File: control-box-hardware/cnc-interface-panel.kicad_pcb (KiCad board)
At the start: 4 copper layers, 94.6 x 73.7 mm, 52 parts, among them J1 USB_B_Mini, J2 SWD_DAPLINK, J3 3V3-OUT, J4 5V-OUT, J5 GND-OUT, J6 IO-A, J7 IO-B, J8 I2C, SW1 BOOT0, SW2 RESET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

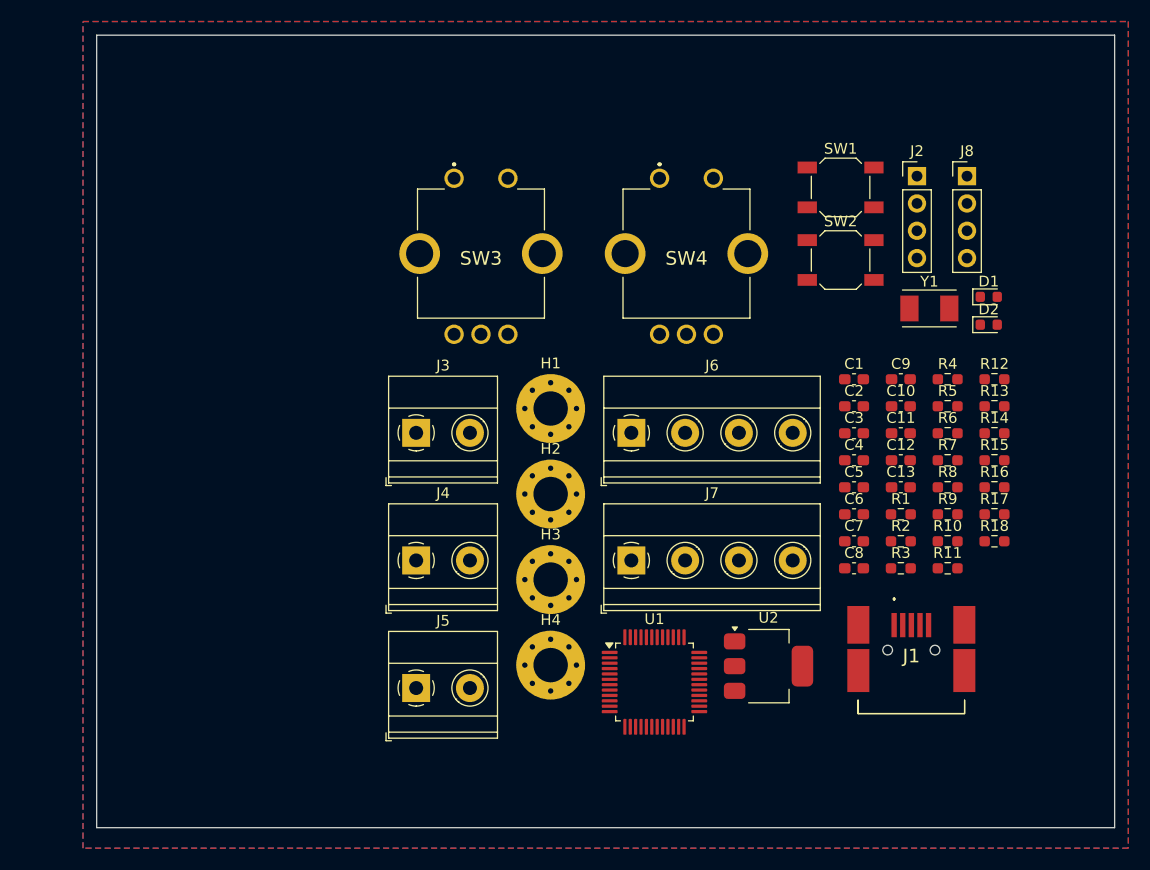
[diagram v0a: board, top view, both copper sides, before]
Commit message: Finish laying out CNC encoders PCB
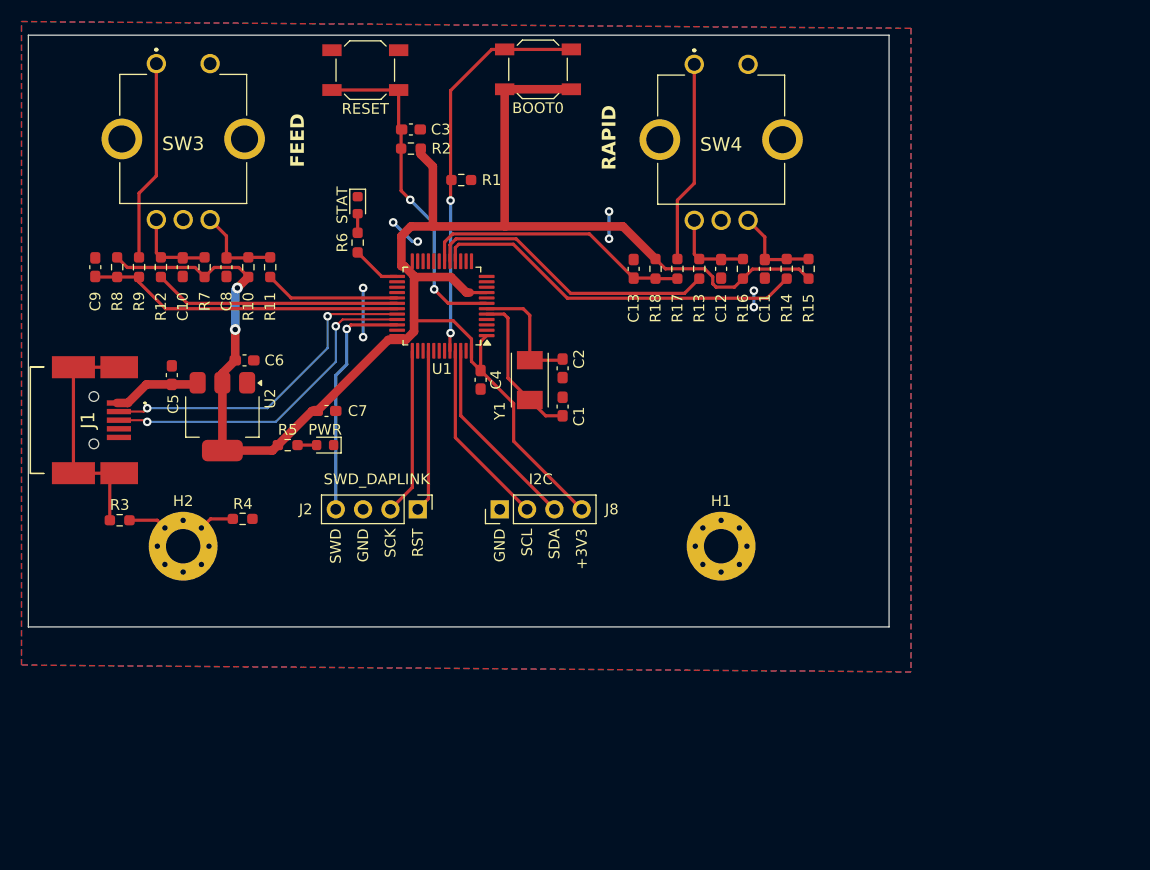
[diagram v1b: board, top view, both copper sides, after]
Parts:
- removed H3, H4: ~, MountingHole:MountingHole_3.2mm_M3_Pad_Via
- removed J3: 3V3-OUT, TerminalBlock_Phoenix:TerminalBlock_Phoenix_MKDS-1,5-2_1x02_P5.00mm_Horizontal
- removed J4: 5V-OUT, TerminalBlock_Phoenix:TerminalBlock_Phoenix_MKDS-1,5-2_1x02_P5.00mm_Horizontal
- removed J5: GND-OUT, TerminalBlock_Phoenix:TerminalBlock_Phoenix_MKDS-1,5-2_1x02_P5.00mm_Horizontal
- removed J6: IO-A, TerminalBlock_Phoenix:TerminalBlock_Phoenix_MKDS-1,5-4_1x04_P5.00mm_Horizontal
- removed J7: IO-B, TerminalBlock_Phoenix:TerminalBlock_Phoenix_MKDS-1,5-4_1x04_P5.00mm_Horizontal
- moved J1 80.7 mm to (82.8, 87.2), turned to -90 degrees
- moved R8 79.9 mm to (86.4, 73.0), turned to -90 degrees
- moved R9 78.6 mm to (88.4, 73.0), turned to 90 degrees
- moved R12 78.2 mm to (90.4, 73.0), turned to 90 degrees
- moved C9 75.6 mm to (84.3, 73.0), turned to 90 degrees
- moved R3 72.7 mm to (86.6, 96.5)
- moved R7 71.4 mm to (94.5, 73.0), turned to 90 degrees
- moved R10 69.8 mm to (98.6, 73.0), turned to 90 degrees
- moved R11 68.9 mm to (100.6, 73.0), turned to 90 degrees
- moved C10 68.0 mm to (92.5, 73.0), turned to -90 degrees
- moved R4 66.8 mm to (98.0, 96.4), turned to 180 degrees
- moved C8 64.7 mm to (96.5, 73.0), turned to -90 degrees
- moved C5 64.3 mm to (91.4, 83.0), turned to 90 degrees
- moved D1 63.2 mm to (105.7, 89.5), turned to 180 degrees
- moved R5 61.4 mm to (102.2, 89.5)
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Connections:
- C3 pad 1: Net-(C3-Pad1) -> Net-(U1-NRST)
- H1 pad 1: CASE -> unconnected-(H1-Pad1)
- J2 pad 1: /SWD -> /RST
- J2 pad 4: /RST -> /SWD
- J8 pad 2: /I2C_SDA -> /I2C_SCL
- J8 pad 3: /I2C_SCL -> /I2C_SDA
- R2 pad 2: Net-(C3-Pad1) -> Net-(U1-NRST)
- SW2 pad 2: Net-(C3-Pad1) -> Net-(U1-NRST)
- U1 pad 10: Net-(J6-Pin_1) -> unconnected-(U1-PA0-Pad10)
- U1 pad 11: Net-(J6-Pin_2) -> unconnected-(U1-PA1-Pad11)
- U1 pad 12: Net-(J6-Pin_3) -> unconnected-(U1-PA2-Pad12)
- U1 pad 13: Net-(J6-Pin_4) -> unconnected-(U1-PA3-Pad13)
- U1 pad 15: /RAPID_RESET -> unconnected-(U1-PA5-Pad15)
- U1 pad 16: /RAPID_A -> /RAPID_B
- U1 pad 17: /RAPID_B -> /RAPID_A
- U1 pad 18: Net-(J7-Pin_1) -> /RAPID_RESET
- U1 pad 19: Net-(J7-Pin_2) -> unconnected-(U1-PB1-Pad19)
- U1 pad 20: Net-(J7-Pin_3) -> unconnected-(U1-PB2-Pad20)
- U1 pad 29: /FEED_A -> /FEED_B
- U1 pad 30: /FEED_B -> /FEED_A
- U1 pad 39: Net-(J7-Pin_4) -> unconnected-(U1-PB3-Pad39)
- U1 pad 7: GND -> Net-(U1-NRST)
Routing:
- net +3V3: track 0.00 -> 168.3 mm, vias 0 -> 2
- net Net-(U1-BOOT0): track 0.00 -> 37.0 mm, vias 0 -> 2
- net /RAPID_B: track 0.00 -> 35.0 mm
- net /D+: track 0.00 -> 32.0 mm, vias 0 -> 2
- net Net-(U1-NRST): track 0.00 -> 31.6 mm, vias 0 -> 2
- net /D-: track 0.00 -> 31.5 mm, vias 0 -> 2
- net /FEED_RESET: track 0.00 -> 29.6 mm
- net /RAPID_A: track 0.00 -> 27.6 mm
- net /RAPID_RESET: track 0.00 -> 25.5 mm
- net Net-(J1-Shield): track 0.00 -> 23.1 mm
- net /FEED_A: track 0.00 -> 23.0 mm
- net /SWD: track 0.00 -> 22.0 mm, vias 0 -> 1
- net Net-(R17-Pad2): track 0.00 -> 18.7 mm
- net Net-(R9-Pad2): track 0.00 -> 18.7 mm
- net /I2C_SDA: track 0.00 -> 18.3 mm
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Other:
- board size 94.6 x 73.7 mm -> 80 x 55 mm
- copper layers 4 -> 2
- board text added: "+3V3"
- board text added: "GND"
- board text added: "RST"
- board text added: "SCK"
- board text added: "SCL"
- board text added: "SDA"
- board text added: "SWD"

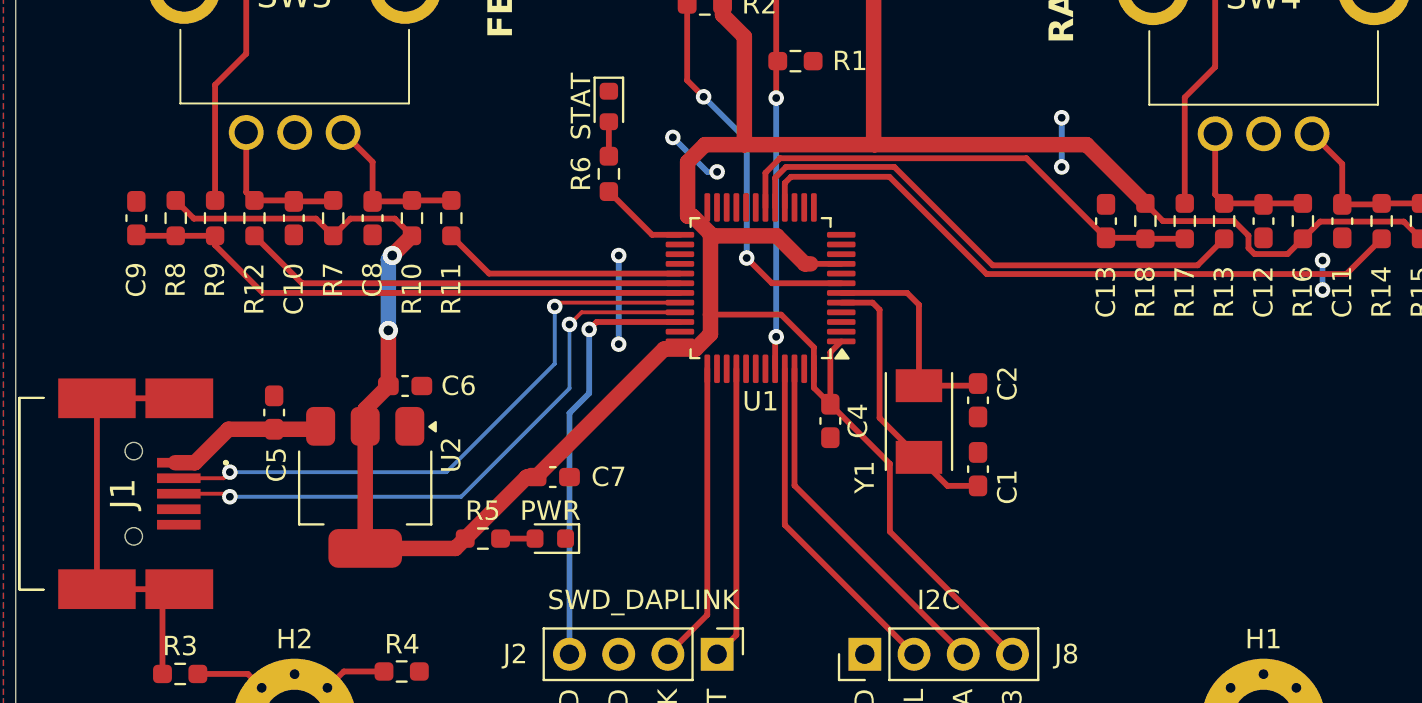
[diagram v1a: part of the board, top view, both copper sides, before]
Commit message: Fix control box PCB issues, add USB connector to BOM
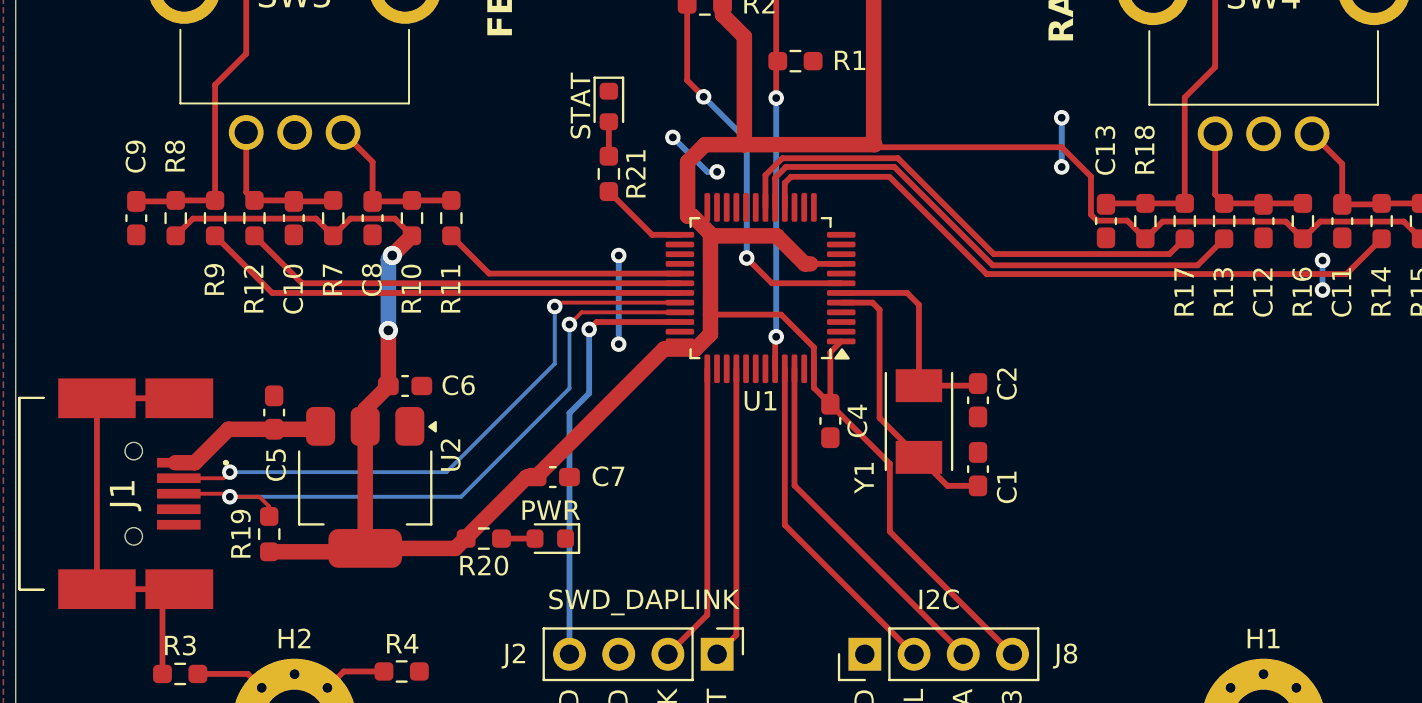
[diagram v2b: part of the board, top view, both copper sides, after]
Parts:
- removed R5, R6: 560, Resistor_SMD:R_0603_1608Metric_Pad0.98x0.95mm_HandSolder
- added R19: 1k5, Resistor_SMD:R_0603_1608Metric_Pad0.98x0.95mm_HandSolder, F.Cu at (91.2, 89.3)
- added R20: 1k5, Resistor_SMD:R_0603_1608Metric_Pad0.98x0.95mm_HandSolder, F.Cu at (102.3, 89.5)
- added R21: 1k5, Resistor_SMD:R_0603_1608Metric_Pad0.98x0.95mm_HandSolder, F.Cu at (108.7, 70.7)
- turned C13 to -90 degrees
- turned C9 to -90 degrees
- turned R18 to 90 degrees
- turned R8 to 90 degrees
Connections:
- C13 pad 1: /RAPID_RESET -> Net-(C13-Pad1)
- C9 pad 1: /FEED_RESET -> Net-(C9-Pad1)
- R17 pad 2: Net-(R17-Pad2) -> Net-(C13-Pad1)
- R18 pad 2: /RAPID_RESET -> Net-(C13-Pad1)
- R8 pad 2: /FEED_RESET -> Net-(C9-Pad1)
- R9 pad 2: Net-(R9-Pad2) -> Net-(C9-Pad1)
- SW3 pad S1: Net-(R9-Pad2) -> Net-(C9-Pad1)
- SW4 pad S1: Net-(R17-Pad2) -> Net-(C13-Pad1)
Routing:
- net Net-(C13-Pad1): track 0.00 -> 22.8 mm
- net Net-(C9-Pad1): track 0.00 -> 22.8 mm
- net Net-(R17-Pad2): track 18.7 -> 0.00 mm
- net Net-(R9-Pad2): track 18.7 -> 0.00 mm
- net +3V3: track 168.3 -> 174.2 mm
- net /FEED_RESET: track 29.6 -> 25.2 mm
- net /D+: track 32.0 -> 34.7 mm
- net /RAPID_RESET: track 25.5 -> 26.0 mm
